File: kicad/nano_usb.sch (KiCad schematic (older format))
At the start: 23 parts, among them P4 USB-A-D-RA-30, P5 USB-A-D-RA-30, U10 MIC2506, U11 MIC2506, U8 USB2514B

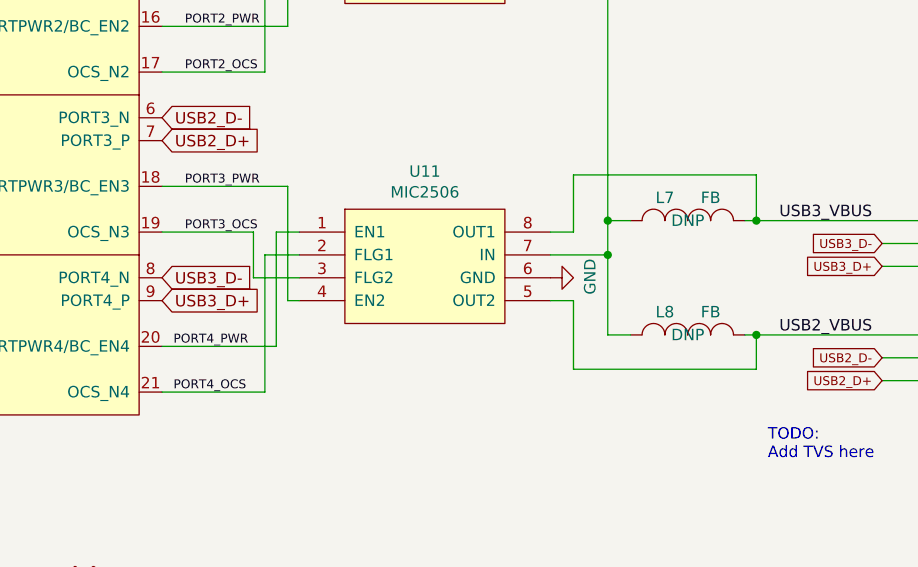
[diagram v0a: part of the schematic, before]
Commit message: layout: move usb hub, improve gpio connections
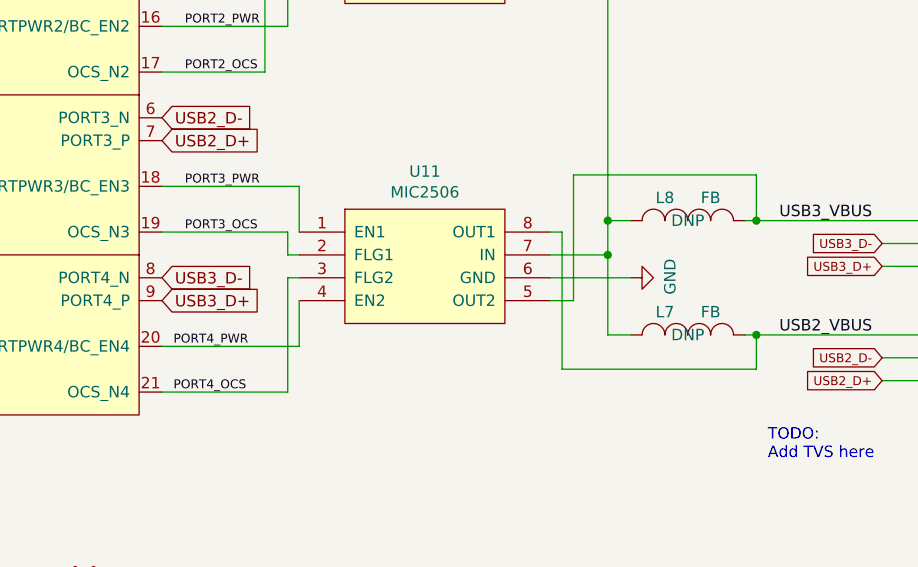
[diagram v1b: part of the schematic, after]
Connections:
- net PORT3_OCS: now also U11.2 (FLG1); no longer U11.3 (FLG2)
- net PORT3_PWR: now also U11.1 (EN1); no longer U11.4 (EN2)
- net PORT4_OCS: now also U11.3 (FLG2); no longer U11.2 (FLG1)
- net PORT4_PWR: now also U11.4 (EN2); no longer U11.1 (EN1)
- net USB2_VBUS: now also L7.2, U11.8 (OUT1); no longer L8.2, U11.5 (OUT2)
- net USB3_VBUS: now also L8.2, U11.5 (OUT2); no longer L7.2, U11.8 (OUT1)
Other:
- moved on the sheet: L7, L8
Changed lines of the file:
@@
 EESchema Schematic File Version 4
-LIBS:nano-cache
 EELAYER 30 0
 EELAYER END
@@
 L nano-rescue:INDUCTOR_SMALL L?
 U 1 1 5C3B97A2
-P 8800 4800
+P 8800 5300
 AR Path="/5C3B97A2" Ref="L?"  Part="1"
 AR Path="/5B867D17/5C3B97A2" Ref="L7"  Part="1"
 AR Path="/5B9F6CF1/5C3B97A2" Ref="L?"  Part="1"
-F 0 "L7" H 8700 4900 50  0000 C CNN
+F 0 "L7" H 8700 5400 50  0000 C CNN
+F 1 "FB" H 8900 5400 50  0000 C CNN
+F 2 "Custom Components:L_0805_narrow" H 8800 5300 50  0001 C CNN
+F 3 "" H 8800 5300 50  0000 C CNN
+F 4 "DNP" H 8800 5300 50  0000 C CNN "DNP"
+	1    8800 5300
+	1    0    0    -1
+$EndComp
+$Comp
+L nano-rescue:INDUCTOR_SMALL L?
+U 1 1 5C3B97A9
+P 8800 4800
+AR Path="/5C3B97A9" Ref="L?"  Part="1"
+AR Path="/5B867D17/5C3B97A9" Ref="L8"  Part="1"
+AR Path="/5B9F6CF1/5C3B97A9" Ref="L?"  Part="1"
+F 0 "L8" H 8700 4900 50  0000 C CNN
 F 1 "FB" H 8900 4900 50  0000 C CNN
 F 2 "Custom Components:L_0805_narrow" H 8800 4800 50  0001 C CNN
@@
 F 4 "DNP" H 8800 4800 50  0000 C CNN "DNP"
 	1    8800 4800
-	1    0    0    -1
-$EndComp
-$Comp
-L nano-rescue:INDUCTOR_SMALL L?
-U 1 1 5C3B97A9
-P 8800 5300
-AR Path="/5C3B97A9" Ref="L?"  Part="1"
-AR Path="/5B867D17/5C3B97A9" Ref="L8"  Part="1"
-AR Path="/5B9F6CF1/5C3B97A9" Ref="L?"  Part="1"
-F 0 "L8" H 8700 5400 50  0000 C CNN
-F 1 "FB" H 8900 5400 50  0000 C CNN
-F 2 "Custom Components:L_0805_narrow" H 8800 5300 50  0001 C CNN
-F 3 "" H 8800 5300 50  0000 C CNN
-F 4 "DNP" H 8800 5300 50  0000 C CNN "DNP"
-	1    8800 5300
 	1    0    0    -1
 $EndComp
@@
 	9100 4600 8300 4600
 Wire Wire Line
-	8300 4600 8300 4850
-Wire Wire Line
-	8300 4850 8200 4850
+	8250 4850 8200 4850
 Connection ~ 9100 4800
 Wire Wire Line
@@
 	9100 5300 9100 5450
 Wire Wire Line
-	9100 5450 8300 5450
-Wire Wire Line
-	8300 5450 8300 5150
+	9100 5450 8250 5450
 Wire Wire Line
 	8300 5150 8200 5150
@@
 L power:GND #PWR?
 U 1 1 5C75C9D8
-P 8200 5050
+P 8550 5050
 AR Path="/5B9F6CF1/5C75C9D8" Ref="#PWR?"  Part="1"
 AR Path="/5B867D17/5C75C9D8" Ref="#PWR078"  Part="1"
-F 0 "#PWR078" H 8200 4800 50  0001 C CNN
-F 1 "GND" H 8205 4877 50  0000 C CNN
-F 2 "" H 8200 5050 50  0001 C CNN
-F 3 "" H 8200 5050 50  0001 C CNN
-	1    8200 5050
+F 0 "#PWR078" H 8550 4800 50  0001 C CNN
+F 1 "GND" H 8555 4877 50  0000 C CNN
+F 2 "" H 8550 5050 50  0001 C CNN
+F 3 "" H 8550 5050 50  0001 C CNN
+	1    8550 5050
 	0    -1   -1   0
 $EndComp
-Wire Wire Line
-	7100 4950 6950 4950
-Wire Wire Line
-	6950 4950 6950 5550
-Wire Wire Line
-	6950 5550 6500 5550
-Wire Wire Line
-	7100 4850 7000 4850
-Wire Wire Line
-	7000 4850 7000 5350
-Wire Wire Line
-	7000 5350 6500 5350
-Wire Wire Line
-	7100 5050 6900 5050
-Wire Wire Line
-	6900 5050 6900 4850
-Wire Wire Line
-	6900 4850 6500 4850
-Wire Wire Line
-	7100 5150 7050 5150
-Wire Wire Line
-	7050 4650 6500 4650
-Wire Wire Line
-	7050 4650 7050 5150
 Text Label 6600 3250 0    39   ~ 0
 PORT1_PWR
@@
 Wire Wire Line
 	4050 2650 4250 2650
+Wire Wire Line
+	8300 4600 8300 5150
+Wire Wire Line
+	8250 4850 8250 5450
+Wire Wire Line
+	7100 4650 7100 4850
+Wire Wire Line
+	6500 4650 7100 4650
+Wire Wire Line
+	7100 4950 7050 4950
+Wire Wire Line
+	7050 4950 7050 4850
+Wire Wire Line
+	6500 4850 7050 4850
+Wire Wire Line
+	7100 5150 7100 5350
+Wire Wire Line
+	6500 5350 7100 5350
+Wire Wire Line
+	7100 5050 7050 5050
+Wire Wire Line
+	7050 5050 7050 5550
+Wire Wire Line
+	6500 5550 7050 5550
+Wire Wire Line
+	8200 5050 8550 5050
 $EndSCHEMATC
